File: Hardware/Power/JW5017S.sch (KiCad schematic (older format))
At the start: 6 parts, among them IC3 DIO6912

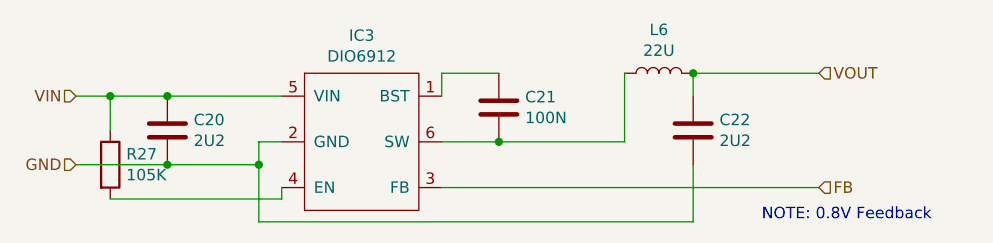
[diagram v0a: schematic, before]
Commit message: Moved MCU Power Supply to Logic Board
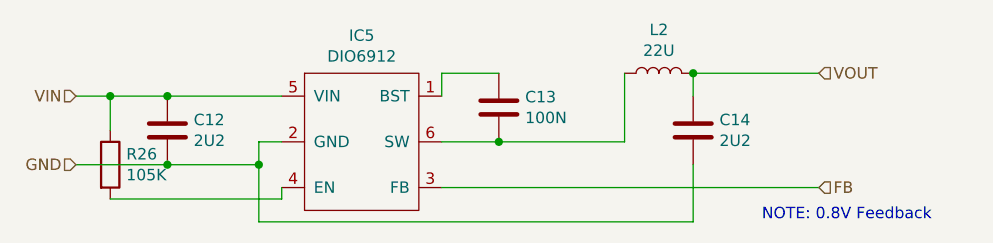
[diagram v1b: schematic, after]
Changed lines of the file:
@@
 AR Path="/5F8DD936/5F8C1478" Ref="IC5"  Part="1"
 AR Path="/5F8C1478" Ref="U?"  Part="1"
-F 0 "IC3" H 5750 4415 50  0000 C CNN
+F 0 "IC5" H 5750 4415 50  0000 C CNN
 F 1 "DIO6912" H 5750 4324 50  0000 C CNN
 F 2 "Package_TO_SOT_SMD:SOT-23-6_Handsoldering" H 5750 4300 50  0001 C CNN
@@
 AR Path="/5F8C9FBB/5F8C353A" Ref="C21"  Part="1"
 AR Path="/5F8DD936/5F8C353A" Ref="C13"  Part="1"
-F 0 "C21" H 6465 3846 50  0000 L CNN
+F 0 "C13" H 6465 3846 50  0000 L CNN
 F 1 "100N" H 6465 3755 50  0000 L CNN
 F 2 "Capacitor_SMD:C_0603_1608Metric_Pad1.05x0.95mm_HandSolder" H 6388 3650 50  0001 C CNN
@@
 AR Path="/5F8C9FBB/5F8C3F06" Ref="L6"  Part="1"
 AR Path="/5F8DD936/5F8C3F06" Ref="L2"  Part="1"
-F 0 "L6" V 7240 3650 50  0000 C CNN
+F 0 "L2" V 7240 3650 50  0000 C CNN
 F 1 "22U" V 7149 3650 50  0000 C CNN
 F 2 "ArduinoLamp:YT0630" H 7050 3650 50  0001 C CNN
@@
 AR Path="/5F8C9FBB/5F8C4C57" Ref="C20"  Part="1"
 AR Path="/5F8DD936/5F8C4C57" Ref="C12"  Part="1"
-F 0 "C20" H 5015 3946 50  0000 L CNN
+F 0 "C12" H 5015 3946 50  0000 L CNN
 F 1 "2U2" H 5015 3855 50  0000 L CNN
 F 2 "Capacitor_SMD:C_0805_2012Metric_Pad1.15x1.40mm_HandSolder" H 4938 3750 50  0001 C CNN
@@
 AR Path="/5F8C9FBB/5F8C53D4" Ref="C22"  Part="1"
 AR Path="/5F8DD936/5F8C53D4" Ref="C14"  Part="1"
-F 0 "C22" H 7315 3946 50  0000 L CNN
+F 0 "C14" H 7315 3946 50  0000 L CNN
 F 1 "2U2" H 7315 3855 50  0000 L CNN
 F 2 "Capacitor_SMD:C_0805_2012Metric_Pad1.15x1.40mm_HandSolder" H 7238 3750 50  0001 C CNN
@@
 AR Path="/5F8DD936/5FA47185" Ref="R26"  Part="1"
 AR Path="/5F8C9FBB/5FA47185" Ref="R27"  Part="1"
-F 0 "R27" H 4720 4096 50  0000 L CNN
+F 0 "R26" H 4720 4096 50  0000 L CNN
 F 1 "105K" H 4720 4005 50  0000 L CNN
 F 2 "Resistor_SMD:R_0603_1608Metric_Pad1.05x0.95mm_HandSolder" V 4580 4050 50  0001 C CNN
